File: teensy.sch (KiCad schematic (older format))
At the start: 1 part

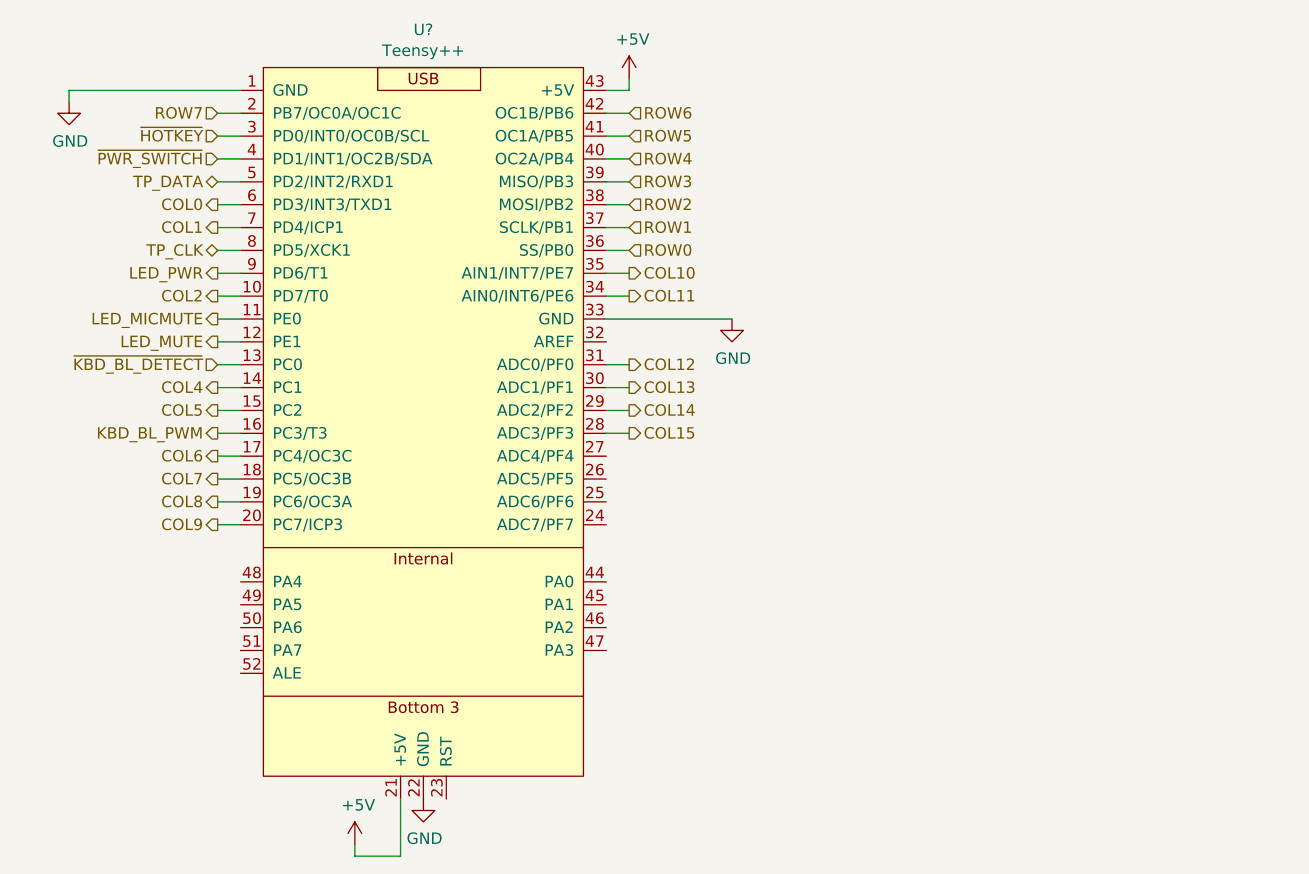
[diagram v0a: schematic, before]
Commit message: Updated footprints and started PCB
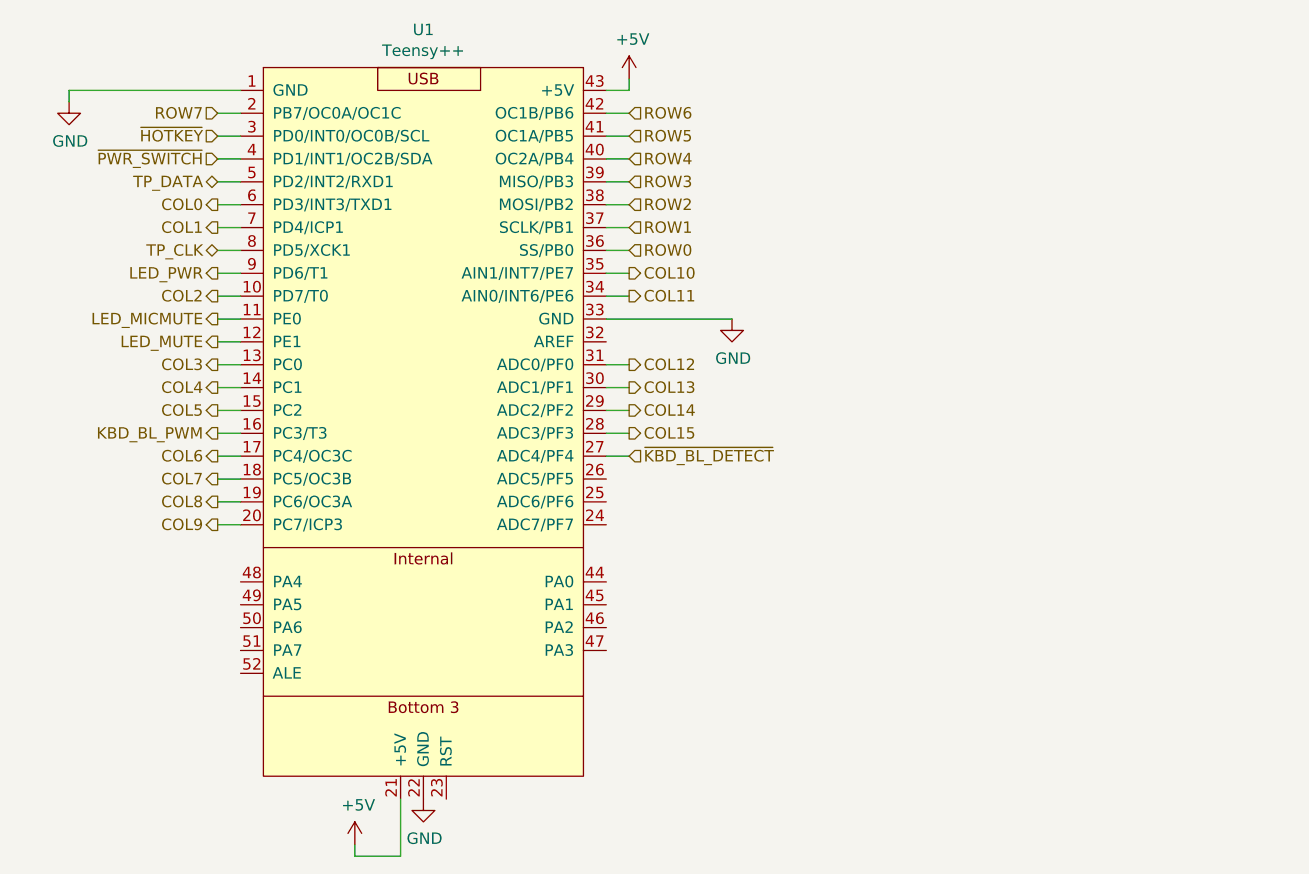
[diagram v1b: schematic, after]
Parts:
- U1: renamed from U?; footprint teensy:Teensy2.0++ -> teensy:Teensy2.0++Pads
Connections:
- net ~KBD_BL_DETECT: now also U1.27 (ADC4/PF4); no longer U1.13 (PC0)
- new net COL3: U1.13 (PC0)
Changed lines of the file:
@@
 $Descr A4 11693 8268
 encoding utf-8
-Sheet 3 3
+Sheet 3 4
 Title ""
 Date ""
@@
 $EndDescr
 $Comp
-L teensy:Teensy++ U?
+L teensy:Teensy++ U1
 U 1 1 5D55F06F
 P 5750 2150
-F 0 "U?" H 5950 2315 50  0000 C CNN
+F 0 "U1" H 5950 2315 50  0000 C CNN
 F 1 "Teensy++" H 5950 2224 50  0000 C CNN
-F 2 "teensy:Teensy2.0++" H 6250 2150 50  0001 C CNN
+F 2 "teensy:Teensy2.0++Pads" H 6250 2150 50  0001 C CNN
 F 3 "" H 6250 2150 50  0001 C CNN
 	1    5750 2150
@@
 	5150 2950 5050 2950
 $Comp
-L power:GND #PWR?
+L power:GND #PWR0121
 U 1 1 5D5631FB
 P 7300 3250
-F 0 "#PWR?" H 7300 3000 50  0001 C CNN
+F 0 "#PWR0121" H 7300 3000 50  0001 C CNN
 F 1 "GND" H 7305 3077 50  0000 C CNN
 F 2 "" H 7300 3250 50  0001 C CNN
@@
 $EndComp
 $Comp
-L power:GND #PWR?
+L power:GND #PWR0122
 U 1 1 5D563633
 P 4400 2300
-F 0 "#PWR?" H 4400 2050 50  0001 C CNN
+F 0 "#PWR0122" H 4400 2050 50  0001 C CNN
 F 1 "GND" H 4405 2127 50  0000 C CNN
 F 2 "" H 4400 2300 50  0001 C CNN
@@
 $EndComp
 $Comp
-L power:+5V #PWR?
+L power:+5V #PWR0123
 U 1 1 5D564B04
 P 6850 2200
-F 0 "#PWR?" H 6850 2050 50  0001 C CNN
+F 0 "#PWR0123" H 6850 2050 50  0001 C CNN
 F 1 "+5V" H 6865 2373 50  0000 C CNN
 F 2 "" H 6850 2200 50  0001 C CNN
@@
 	6850 2250 6850 2200
 $Comp
-L power:GND #PWR?
+L power:GND #PWR0124
 U 1 1 5D565367
 P 5950 5350
-F 0 "#PWR?" H 5950 5100 50  0001 C CNN
+F 0 "#PWR0124" H 5950 5100 50  0001 C CNN
 F 1 "GND" H 5955 5177 50  0000 C CNN
 F 2 "" H 5950 5350 50  0001 C CNN
@@
 $EndComp
 $Comp
-L power:+5V #PWR?
+L power:+5V #PWR0125
 U 1 1 5D566132
 P 5650 5550
-F 0 "#PWR?" H 5650 5400 50  0001 C CNN
+F 0 "#PWR0125" H 5650 5400 50  0001 C CNN
 F 1 "+5V" H 5665 5723 50  0000 C CNN
 F 2 "" H 5650 5550 50  0001 C CNN
@@
 Text HLabel 5050 3750 0    50   Output ~ 0
 KBD_BL_PWM
-Text HLabel 5050 3450 0    50   Input ~ 0
+Text HLabel 6850 3850 2    50   Input ~ 0
 ~KBD_BL_DETECT
 Text HLabel 5050 3050 0    50   Output ~ 0
@@
 Wire Wire Line
 	6750 3750 6850 3750
+Wire Wire Line
+	6750 3850 6850 3850
+Text HLabel 5050 3450 0    50   Output ~ 0
+COL3
 $EndSCHEMATC

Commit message: Routed to 6/6
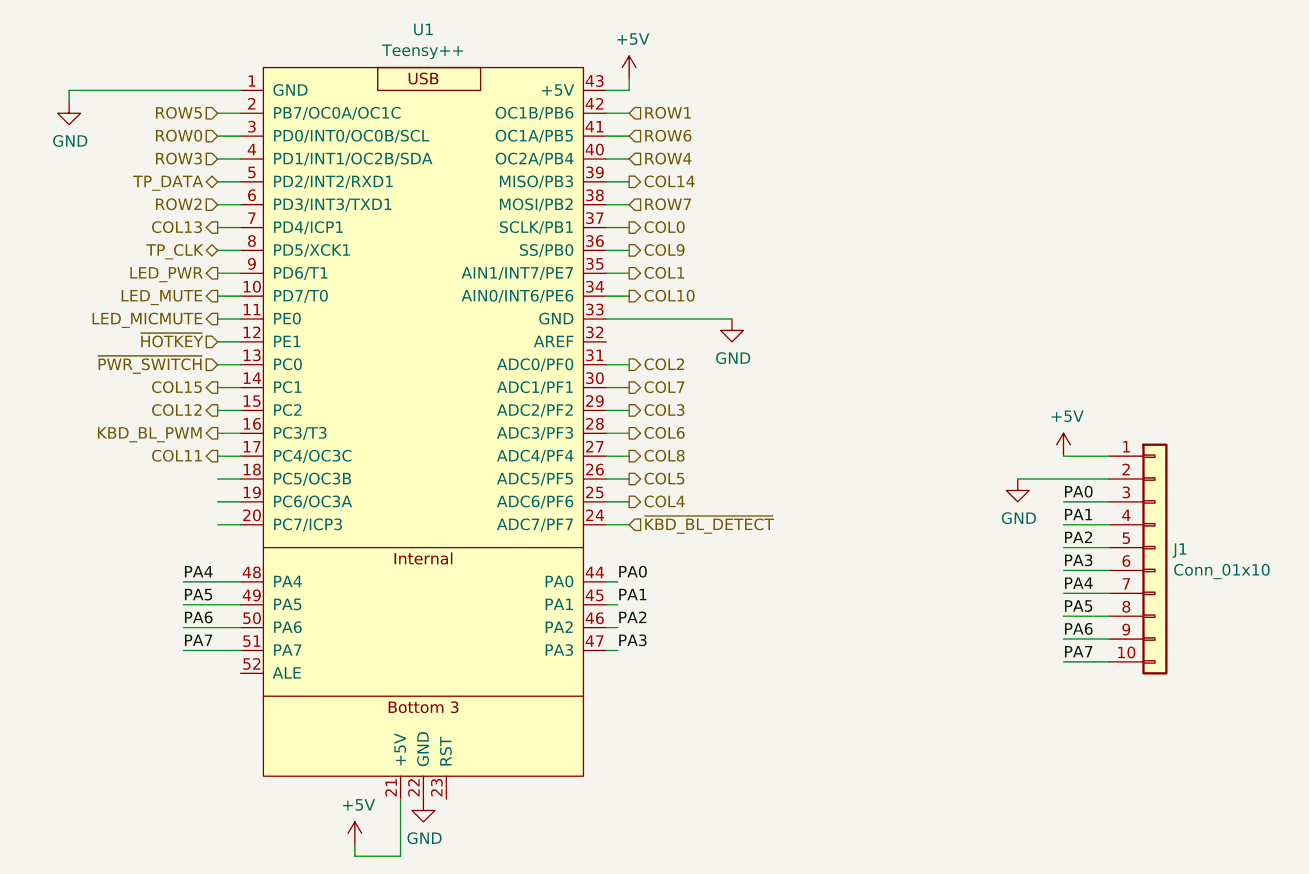
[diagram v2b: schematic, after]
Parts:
- added J1: Conn_01x10, Connector_PinSocket_2.54mm:PinSocket_1x10_P2.54mm_Vertical, symbol Connector_Generic:Conn_01x10
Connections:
- net labels added: PA0, PA1, PA2, PA3, PA4, PA5, PA6, PA7
- wire segments 41 -> 62
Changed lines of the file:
@@
 	1    0    0    -1
 $EndComp
-Text HLabel 6850 2950 2    50   Input ~ 0
+Text HLabel 5050 2450 0    50   Input ~ 0
 ROW0
-Text HLabel 6850 2850 2    50   Input ~ 0
+Text HLabel 6850 2350 2    50   Input ~ 0
 ROW1
-Text HLabel 6850 2750 2    50   Input ~ 0
+Text HLabel 5050 2750 0    50   Input ~ 0
 ROW2
-Text HLabel 6850 2650 2    50   Input ~ 0
+Text HLabel 5050 2550 0    50   Input ~ 0
 ROW3
 Text HLabel 6850 2550 2    50   Input ~ 0
 ROW4
+Text HLabel 5050 2350 0    50   Input ~ 0
+ROW5
 Text HLabel 6850 2450 2    50   Input ~ 0
-ROW5
-Text HLabel 6850 2350 2    50   Input ~ 0
 ROW6
-Text HLabel 5050 2350 0    50   Input ~ 0
+Text HLabel 6850 2750 2    50   Input ~ 0
 ROW7
-Wire Wire Line
-	5050 2350 5150 2350
-Wire Wire Line
-	6850 2350 6750 2350
-Wire Wire Line
-	6850 2450 6750 2450
-Wire Wire Line
-	6750 2550 6850 2550
-Wire Wire Line
-	6850 2650 6750 2650
-Wire Wire Line
-	6750 2750 6850 2750
-Wire Wire Line
-	6850 2850 6750 2850
-Wire Wire Line
-	6750 2950 6850 2950
 Text HLabel 5050 2950 0    50   BiDi ~ 0
 TP_CLK
@@
 Wire Wire Line
 	5850 5600 5850 5350
-Text HLabel 5050 2450 0    50   Input ~ 0
+Text HLabel 5050 3350 0    50   Input ~ 0
 ~HOTKEY
-Text HLabel 5050 2550 0    50   Input ~ 0
+Text HLabel 5050 3450 0    50   Input ~ 0
 ~PWR_SWITCH
 Wire Wire Line
@@
 Text HLabel 5050 3750 0    50   Output ~ 0
 KBD_BL_PWM
-Text HLabel 6850 3850 2    50   Input ~ 0
+Text HLabel 6850 4150 2    50   Input ~ 0
 ~KBD_BL_DETECT
 Text HLabel 5050 3050 0    50   Output ~ 0
@@
 Text HLabel 5050 3250 0    50   Output ~ 0
 LED_MICMUTE
-Text HLabel 5050 3350 0    50   Output ~ 0
+Text HLabel 5050 3150 0    50   Output ~ 0
 LED_MUTE
 Wire Wire Line
@@
 Wire Wire Line
 	5050 3450 5150 3450
-Text HLabel 5050 2750 0    50   Output ~ 0
+Text HLabel 6850 2850 2    50   Output ~ 0
 COL0
+Text HLabel 6850 3050 2    50   Output ~ 0
+COL1
+Text HLabel 6850 3450 2    50   Output ~ 0
+COL2
+Wire Wire Line
+	5050 2750 5150 2750
+Wire Wire Line
+	5150 2850 5050 2850
+Wire Wire Line
+	5150 3150 5050 3150
+Text HLabel 6850 4050 2    50   Output ~ 0
+COL4
+Text HLabel 6850 3950 2    50   Output ~ 0
+COL5
+Text HLabel 6850 3750 2    50   Output ~ 0
+COL6
+Text HLabel 6850 3550 2    50   Output ~ 0
+COL7
+Text HLabel 6850 3850 2    50   Output ~ 0
+COL8
+Text HLabel 6850 2950 2    50   Output ~ 0
+COL9
+Text HLabel 6850 3150 2    50   Output ~ 0
+COL10
+Text HLabel 5050 3850 0    50   Output ~ 0
+COL11
 Text HLabel 5050 2850 0    50   Output ~ 0
-COL1
-Text HLabel 5050 3150 0    50   Output ~ 0
-COL2
-Wire Wire Line
-	5050 2750 5150 2750
-Wire Wire Line
-	5150 2850 5050 2850
-Wire Wire Line
-	5150 3150 5050 3150
+COL13
+Text HLabel 6850 2650 2    50   Output ~ 0
+COL14
 Text HLabel 5050 3550 0    50   Output ~ 0
-COL4
+COL15
+Wire Wire Line
+	6750 3250 7300 3250
+Wire Wire Line
+	5050 3550 5150 3550
+Wire Wire Line
+	5150 3650 5050 3650
+Wire Wire Line
+	5050 3850 5150 3850
+Wire Wire Line
+	5150 3950 5050 3950
+Wire Wire Line
+	5050 4050 5150 4050
+Wire Wire Line
+	5150 4150 5050 4150
+Wire Wire Line
+	6850 3050 6750 3050
+Wire Wire Line
+	6750 3150 6850 3150
+Wire Wire Line
+	6850 3450 6750 3450
+Wire Wire Line
+	6750 3550 6850 3550
+Wire Wire Line
+	6850 3650 6750 3650
+Wire Wire Line
+	6750 3750 6850 3750
+Wire Wire Line
+	6750 3850 6850 3850
+Text HLabel 6850 3650 2    50   Output ~ 0
+COL3
+Wire Wire Line
+	6850 2550 6750 2550
+Wire Wire Line
+	6850 2650 6750 2650
+Wire Wire Line
+	6750 2750 6850 2750
+Wire Wire Line
+	6750 2850 6850 2850
+Wire Wire Line
+	6850 2950 6750 2950
 Text HLabel 5050 3650 0    50   Output ~ 0
-COL5
-Text HLabel 5050 3850 0    50   Output ~ 0
-COL6
-Text HLabel 5050 3950 0    50   Output ~ 0
-COL7
-Text HLabel 5050 4050 0    50   Output ~ 0
-COL8
-Text HLabel 5050 4150 0    50   Output ~ 0
-COL9
-Text HLabel 6850 3050 2    50   Output ~ 0
-COL10
-Text HLabel 6850 3150 2    50   Output ~ 0
-COL11
-Text HLabel 6850 3450 2    50   Output ~ 0
 COL12
-Text HLabel 6850 3550 2    50   Output ~ 0
-COL13
-Text HLabel 6850 3650 2    50   Output ~ 0
-COL14
-Text HLabel 6850 3750 2    50   Output ~ 0
-COL15
-Wire Wire Line
-	6750 3250 7300 3250
-Wire Wire Line
-	5050 3550 5150 3550
-Wire Wire Line
-	5150 3650 5050 3650
-Wire Wire Line
-	5050 3850 5150 3850
-Wire Wire Line
-	5150 3950 5050 3950
-Wire Wire Line
-	5050 4050 5150 4050
-Wire Wire Line
-	5150 4150 5050 4150
-Wire Wire Line
-	6850 3050 6750 3050
-Wire Wire Line
-	6750 3150 6850 3150
-Wire Wire Line
-	6850 3450 6750 3450
-Wire Wire Line
-	6750 3550 6850 3550
-Wire Wire Line
-	6850 3650 6750 3650
-Wire Wire Line
-	6750 3750 6850 3750
-Wire Wire Line
-	6750 3850 6850 3850
-Text HLabel 5050 3450 0    50   Output ~ 0
-COL3
+Wire Wire Line
+	6750 2350 6850 2350
+Wire Wire Line
+	6750 2450 6850 2450
+Wire Wire Line
+	6750 3950 6850 3950
+Wire Wire Line
+	6850 4050 6750 4050
+Wire Wire Line
+	6750 4150 6850 4150
+Wire Wire Line
+	5050 2350 5150 2350
+$Comp
+L Connector_Generic:Conn_01x10 J1
+U 1 1 5D4FF33B
+P 9150 4250
+F 0 "J1" H 9230 4242 50  0000 L CNN
+F 1 "Conn_01x10" H 9230 4151 50  0000 L CNN
+F 2 "Connector_PinSocket_2.54mm:PinSocket_1x10_P2.54mm_Vertical" H 9150 4250 50  0001 C CNN
+F 3 "~" H 9150 4250 50  0001 C CNN
+	1    9150 4250
+	1    0    0    -1
+$EndComp
+Text Label 6800 4400 0    50   ~ 0
+PA0
+Text Label 6800 4500 0    50   ~ 0
+PA1
+Text Label 6800 4600 0    50   ~ 0
+PA2
+Text Label 6800 4700 0    50   ~ 0
+PA3
+Text Label 4900 4400 0    50   ~ 0
+PA4
+Text Label 4900 4500 0    50   ~ 0
+PA5
+Text Label 4900 4600 0    50   ~ 0
+PA6
+Text Label 4900 4700 0    50   ~ 0
+PA7
+Wire Wire Line
+	4900 4400 5150 4400
+Wire Wire Line
+	5150 4500 4900 4500
+Wire Wire Line
+	4900 4600 5150 4600
+Wire Wire Line
+	4900 4700 5150 4700
+Wire Wire Line
+	6750 4400 6800 4400
+Wire Wire Line
+	6800 4500 6750 4500
+Wire Wire Line
+	6800 4600 6750 4600
+Wire Wire Line
+	6800 4700 6750 4700
+Text Label 8750 4050 0    50   ~ 0
+PA0
+Text Label 8750 4150 0    50   ~ 0
+PA1
+Text Label 8750 4250 0    50   ~ 0
+PA2
+Text Label 8750 4350 0    50   ~ 0
+PA3
+Text Label 8750 4450 0    50   ~ 0
+PA4
+Text Label 8750 4550 0    50   ~ 0
+PA5
+Text Label 8750 4650 0    50   ~ 0
+PA6
+Text Label 8750 4750 0    50   ~ 0
+PA7
+$Comp
+L power:+5V #PWR01
+U 1 1 5D5093DD
+P 8750 3850
+F 0 "#PWR01" H 8750 3700 50  0001 C CNN
+F 1 "+5V" H 8765 4023 50  0000 C CNN
+F 2 "" H 8750 3850 50  0001 C CNN
+F 3 "" H 8750 3850 50  0001 C CNN
+	1    8750 3850
+	1    0    0    -1
+$EndComp
+Wire Wire Line
+	8750 4650 8950 4650
+Wire Wire Line
+	8950 4550 8750 4550
+Wire Wire Line
+	8750 4450 8950 4450
+Wire Wire Line
+	8950 4350 8750 4350
+Wire Wire Line
+	8750 4250 8950 4250
+Wire Wire Line
+	8950 4150 8750 4150
+Wire Wire Line
+	8750 4050 8950 4050
+Wire Wire Line
+	8750 4750 8950 4750
+Wire Wire Line
+	8750 3850 8950 3850
+$Comp
+L power:GND #PWR?
+U 1 1 5D524C67
+P 8550 3950
+F 0 "#PWR?" H 8550 3700 50  0001 C CNN
+F 1 "GND" H 8555 3777 50  0000 C CNN
+F 2 "" H 8550 3950 50  0001 C CNN
+F 3 "" H 8550 3950 50  0001 C CNN
+	1    8550 3950
+	1    0    0    -1
+$EndComp
+Wire Wire Line
+	8550 3950 8950 3950
 $EndSCHEMATC
